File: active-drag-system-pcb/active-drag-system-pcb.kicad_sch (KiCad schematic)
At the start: 39 parts, among them J1 USB_B_Micro, J2 Conn_01x02, J3 Conn_02x18_Odd_Even, J4 Conn_02x18_Odd_Even, U1 NCP1117-3.3_SOT223, U2 W25Q128JVS, U3 RP2040, U4 CYW43439KUBGT, U5 ADXL375BCCZ, U6 IIM-42653, U7 LSM6DSV16XTR, U8 NCP1117ST50T3G, Y1 ABM8-272-T3

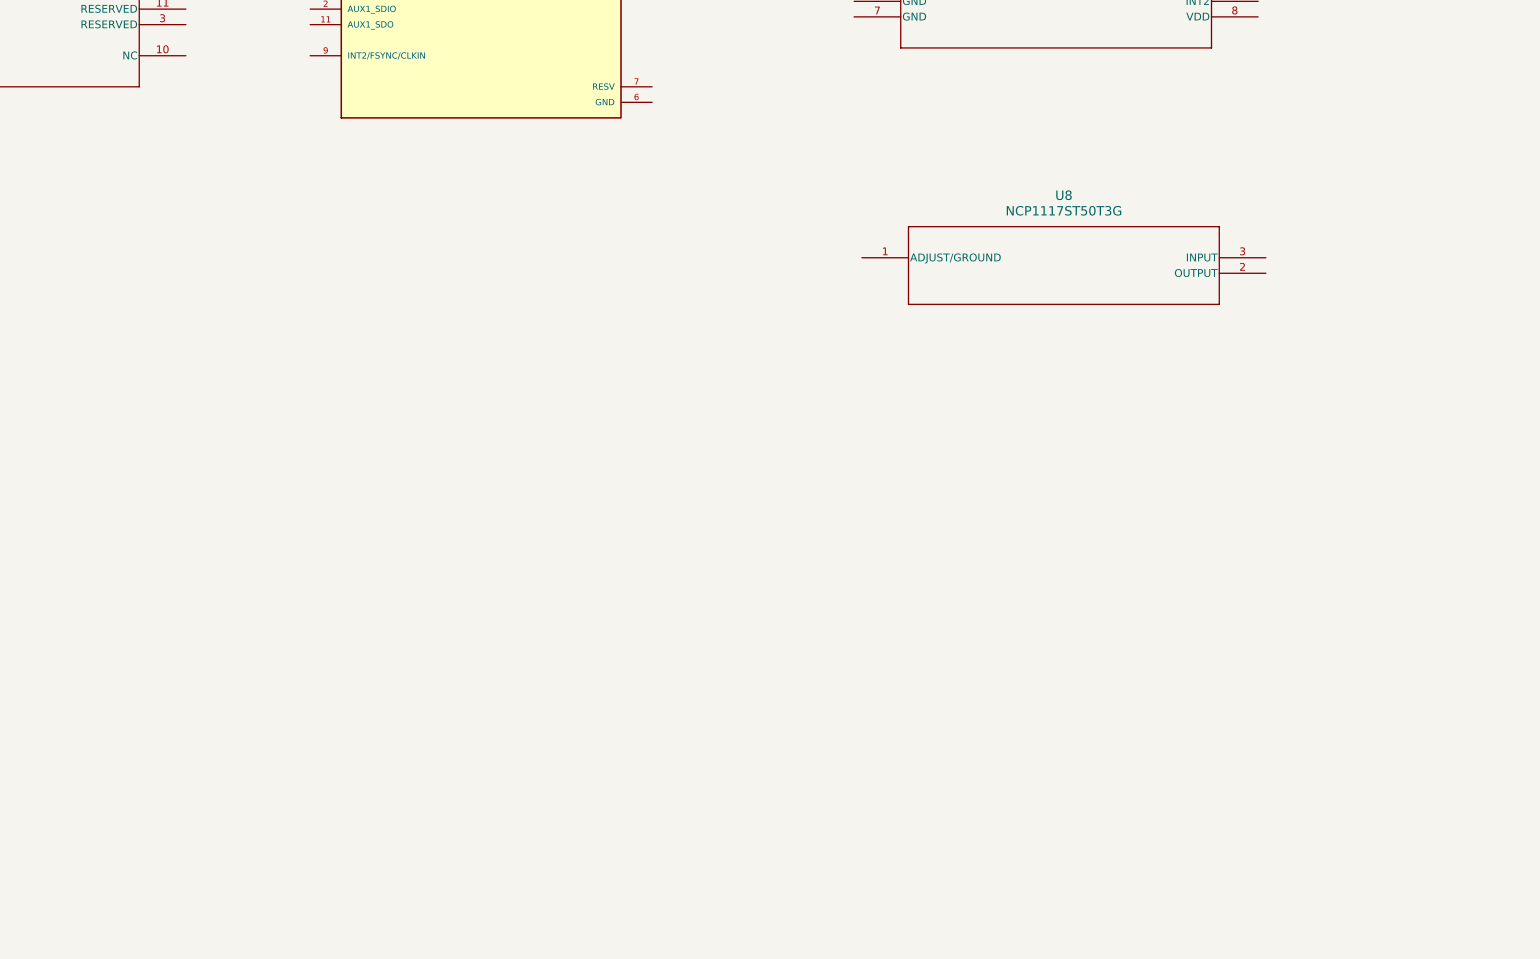
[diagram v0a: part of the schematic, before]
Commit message: 3.3v ldo and 5v+8.4v switching schematic
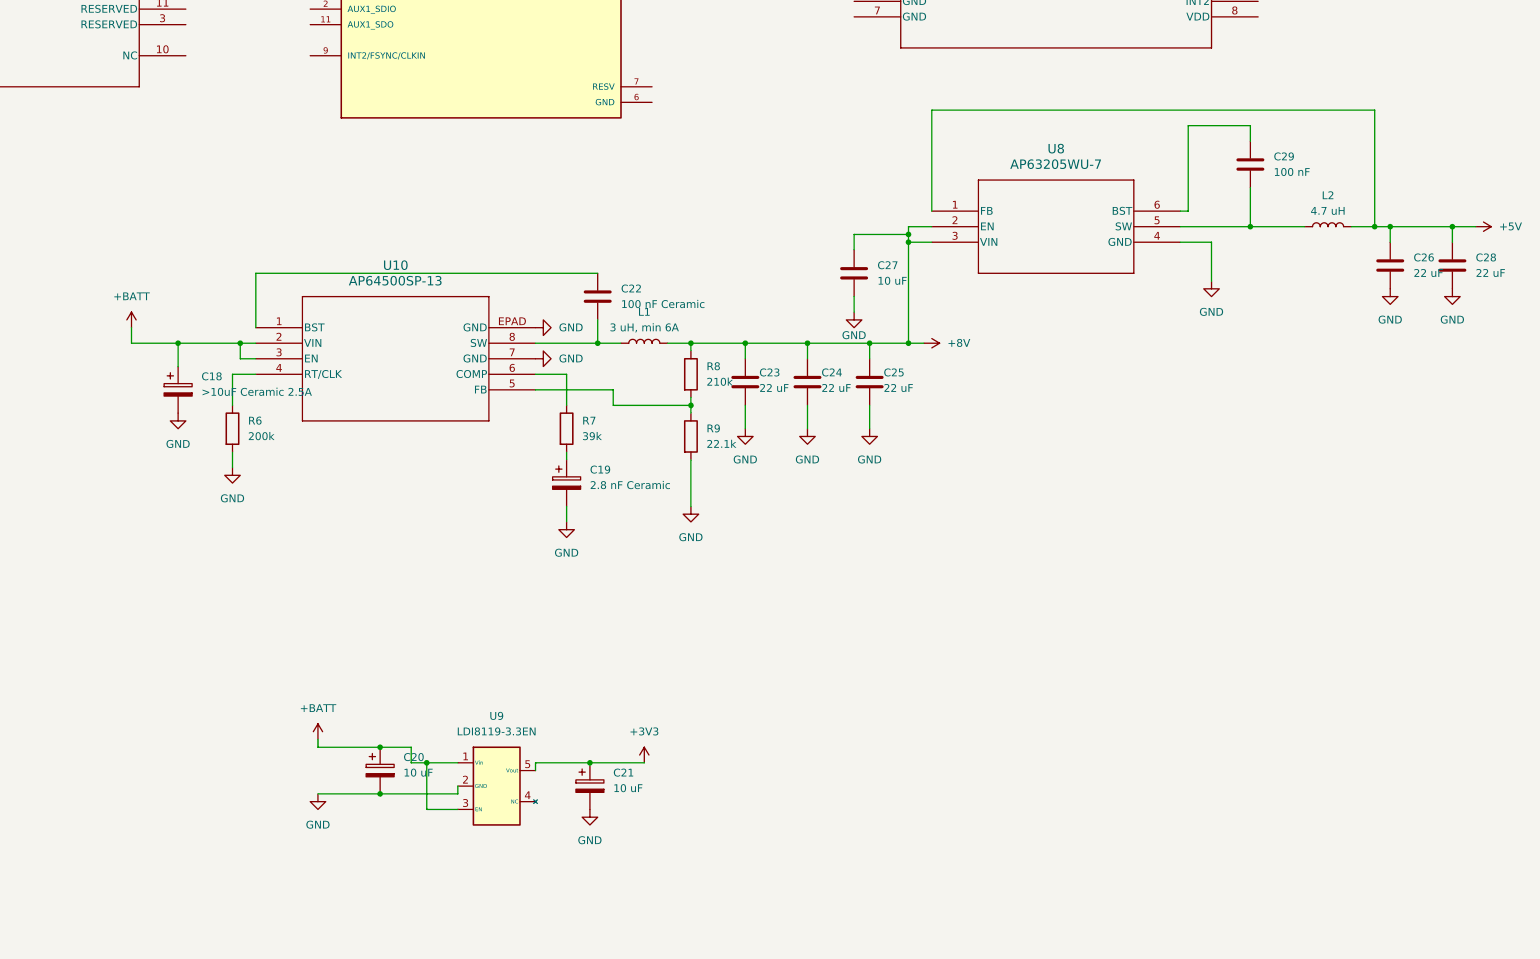
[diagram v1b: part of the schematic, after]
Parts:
- removed U8: NCP1117ST50T3G, SOT223-3_ONS, symbol ADS_Library:NCP1117ST50T3G
- added C18: >10uF Ceramic 2.5A, symbol Device:C_Polarized
- added C19: 2.8 nF Ceramic, symbol Device:C_Polarized
- added C20, C21: 10 uF, symbol Device:C_Polarized
- added C22: 100 nF Ceramic, symbol Device:C
- added C23, C24, C25, C26, C28: 22 uF, symbol Device:C
- added C27: 10 uF, symbol Device:C
- added C29: 100 nF, symbol Device:C
- added L1: 3 uH, min 6A, symbol Device:L
- added L2: 4.7 uH, symbol Device:L
- added R6: 200k, symbol Device:R
- added R7: 39k, symbol Device:R
- added R8: 210k, symbol Device:R
- added R9: 22.1k, symbol Device:R
- added U10: AP64500SP-13, SO-8EP_DIO, symbol ADS_Library:AP64500SP-13
- added U8: AP63205WU-7, SOIC_05WU-7_DIO, symbol ADS_Library:AP63205WU-7
- added U9: LDI8119-3.3EN, symbol ADS_Library:LDI8119-3.3EN
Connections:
- net +3V3: now also C21.1, U9.5 (Vout)
- net GND: now also C18.2, C19.2, C20.2, C21.2, C23.2, C24.2, C25.2, C26.2, C27.2, C28.2, R6.2, R9.2, U10.7 (GND), U10.EPAD (GND), U8.4 (GND), U9.2 (GND)
- new net: R8.2, R9.1, U10.5 (FB)
- new net: C22.1, U10.1 (BST)
- new net: C22.2, L1.1, U10.8 (SW)
- new net: R7.1, U10.6 (COMP)
- new net: C19.1, R7.2
- new net: C29.2, L2.1, U8.5 (SW)
- new net: C29.1, U8.6 (BST)
- new net: R6.1, U10.4 (RT/CLK)
- new net +5V: C26.1, C28.1, L2.2, U8.1 (FB)
- new net +8V: C23.1, C24.1, C25.1, C27.1, L1.2, R8.1, U8.2 (EN), U8.3 (VIN)
- new net +BATT: C18.1, C20.1, U10.2 (VIN), U10.3 (EN), U9.1 (Vin), U9.3 (EN)

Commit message: fixed power nets
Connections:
- net +5V: now also C20.1, U9.1 (Vin), U9.3 (EN)
- net +8V: no longer C27.1, U8.2 (EN), U8.3 (VIN)
- net +BATT: now also C27.1, U8.2 (EN), U8.3 (VIN); no longer C20.1, U9.1 (Vin), U9.3 (EN)
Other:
- moved on the sheet: C26, C27, C28, C29, L2, U8

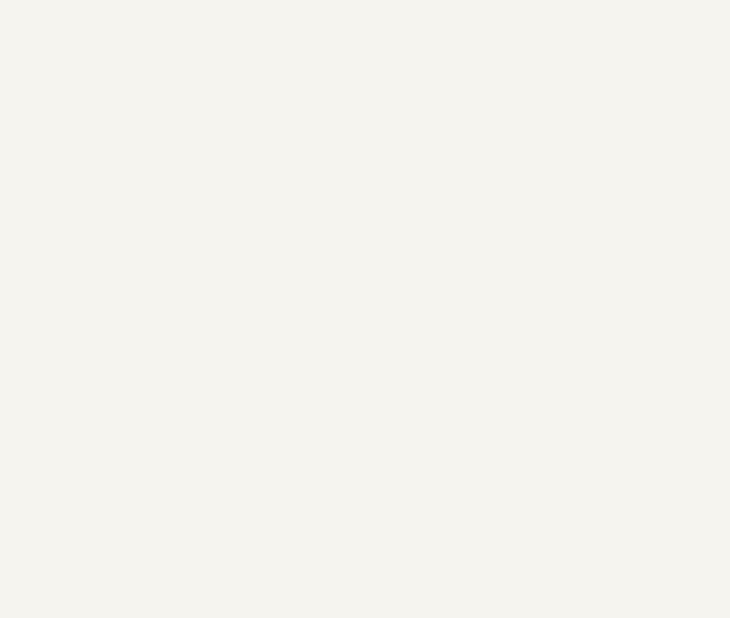
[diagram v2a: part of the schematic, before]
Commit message: First Phase Motor Control
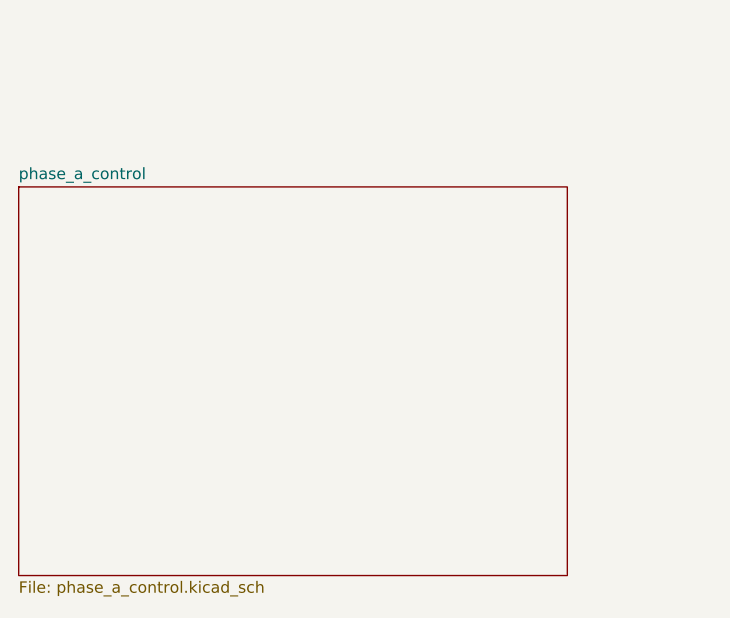
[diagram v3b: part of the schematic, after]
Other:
- added sheet phase_a_control (phase_a_control.kicad_sch)
- company: (none) -> Rocketry at Virginia Tech
- title: (none) -> Active Drag System

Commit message: Add other two phases; remove CYW43 for scope reasons
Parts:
- removed U4: CYW43439KUBGT, SG-XFWLB-63-800, symbol ADS_Library:CYW43439KUBGT
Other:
- added sheet phase_b_control (phase_b_control.kicad_sch)
- added sheet phase_c_control (phase_c_control.kicad_sch)
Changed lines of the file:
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@@
-	)
-	(symbol
-		(lib_id "ADS_Library:CYW43439KUBGT")
-		(at 379.73 66.04 0)
-		(unit 1)
-		(exclude_from_sim no)
-		(in_bom yes)
-		(on_board yes)
-		(dnp no)
-		(fields_autoplaced yes)
-		(property "Reference" "U4"
-			(at 435.61 55.88 0)
-			(effects
-				(font
-					(size 1.524 1.524)
-				)
-			)
-		)
-		(property "Value" "CYW43439KUBGT"
-			(at 435.61 58.42 0)
-			(effects
-				(font
-					(size 1.524 1.524)
-				)
-			)
-		)
-		(property "Footprint" "SG-XFWLB-63-800"
-			(at 379.73 66.04 0)
-			(effects
-				(font
-					(size 1.27 1.27)
-					(italic yes)
-				)
-				(hide yes)
-			)
-		)
-		(property "Datasheet" "CYW43439KUBGT"
-			(at 379.73 66.04 0)
-			(effects
-				(font
-					(size 1.27 1.27)
-					(italic yes)
-				)
-				(hide yes)
-			)
-		)
-		(property "Description" ""
-			(at 379.73 66.04 0)
-			(effects
-				(font
-					(size 1.27 1.27)
-				)
-				(hide yes)
-			)
-		)
-		(pin "G4"
-		)
-		(pin "A1"
-		)
-		(pin "A5"
-		)
-		(pin "J3"
-		)
-		(pin "H1"
-		)
-		(pin "F5"
-		)
-		(pin "C1"
-		)
-		(pin "H2"
-		)
-		(pin "A7"
-		)
-		(pin "C2"
-		)
-		(pin "C6"
-		)
-		(pin "D2"
-		)
-		(pin "C3"
-		)
-		(pin "E1"
-		)
-		(pin "F1"
-		)
-		(pin "D3"
-		)
-		(pin "G1"
-		)
-		(pin "G6"
-		)
-		(pin "C4"
-		)
-		(pin "A6"
-		)
-		(pin "B6"
-		)
-		(pin "B7"
-		)
-		(pin "D6"
-		)
-		(pin "C7"
-		)
-		(pin "E2"
-		)
-		(pin "E3"
-		)
-		(pin "E7"
-		)
-		(pin "F2"
-		)
-		(pin "F6"
-		)
-		(pin "H3"
-		)
-		(pin "H4"
-		)
-		(pin "B5"
-		)
-		(pin "A2"
-		)
-		(pin "G2"
-		)
-		(pin "D4"
-		)
-		(pin "B2"
-		)
-		(pin "E6"
-		)
-		(pin "B1"
-		)
-		(pin "B4"
-		)
-		(pin "F7"
-		)
-		(pin "M4"
-		)
-		(pin "L5"
-		)
-		(pin "M1"
-		)
-		(pin "K2"
-		)
-		(pin "K6"
-		)
-		(pin "J1"
-		)
-		(pin "J6"
-		)
-		(pin "L3"
-		)
-		(pin "J7"
-		)
-		(pin "J2"
-		)
-		(pin "M3"
-		)
-		(pin "K1"
-		)
-		(pin "L4"
-		)
-		(pin "H6"
-		)
-		(pin "M5"
-		)
-		(pin "H7"
-		)
-		(pin "J5"
-		)
-		(pin "L7"
-		)
-		(pin "L2"
-		)
-		(pin "M2"
-		)
-		(pin "M7"
-		)
-		(pin "L6"
-		)
-		(pin "M6"
-		)
-		(instances
-			(project ""
-				(path "/bbbb29dc-aa75-4226-931e-5c4f0b0fc0d6"
-					(reference "U4")
-					(unit 1)
-				)
-			)
-		)
 	)
 	(symbol
@@
 				)
 			)
+		)
+	)
+	(sheet
+		(at 172.72 444.5)
+		(size 60.96 43.18)
+		(fields_autoplaced yes)
+		(stroke
+			(width 0.1524)
+			(type solid)
+		)
+		(fill
+			(color 0 0 0 0.0000)
+		)
+		(property "Sheetname" "phase_b_control"
+			(at 172.72 443.7884 0)
+			(effects
+				(font
+					(size 1.27 1.27)
+				)
+				(justify left bottom)
+			)
+		)
+		(property "Sheetfile" "phase_b_control.kicad_sch"
+			(at 172.72 488.2646 0)
+			(effects
+				(font
+					(size 1.27 1.27)
+				)
+				(justify left top)
+			)
+		)
+		(instances
+			(project "active-drag-system-pcb"
+				(path "/bbbb29dc-aa75-4226-931e-5c4f0b0fc0d6"
+					(page "3")
+				)
+			)
+		)
+	)
+	(sheet
+		(at 247.65 444.5)
+		(size 60.96 43.18)
+		(fields_autoplaced yes)
+		(stroke
+			(width 0.1524)
+			(type solid)
+		)
+		(fill
+			(color 0 0 0 0.0000)
+		)
+		(property "Sheetname" "phase_c_control"
+			(at 247.65 443.7884 0)
+			(effects
+				(font
+					(size 1.27 1.27)
+				)
+				(justify left bottom)
+			)
+		)
+		(property "Sheetfile" "phase_c_control.kicad_sch"
+			(at 247.65 488.2646 0)
+			(effects
+				(font
+					(size 1.27 1.27)
+				)
+				(justify left top)
+			)
+		)
+		(property "Field2" ""
+			(at 247.65 444.5 0)
+			(effects
+				(font
+					(size 1.27 1.27)
+				)
+				(hide yes)
+			)
+		)
+		(instances
+			(project "active-drag-system-pcb"
+				(path "/bbbb29dc-aa75-4226-931e-5c4f0b0fc0d6"
+					(page "4")
+				)
+			)

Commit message: Swapped out regulators for higher current output; removed 8.4 V regulator; now two grounds (power and analog)
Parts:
- removed C17: 10u, Capacitor_SMD:C_0805_2012Metric, symbol Device:C
- removed C18: >10uF Ceramic 2.5A, symbol Device:C_Polarized
- removed C19: 2.8 nF Ceramic, symbol Device:C_Polarized
- removed C20, C21: 10 uF, symbol Device:C_Polarized
- removed C22: 100 nF Ceramic, symbol Device:C
- removed C23, C24, C25, C26, C28: 22 uF, symbol Device:C
- removed C27: 10 uF, symbol Device:C
- removed C29: 100 nF, symbol Device:C
- removed J3, J4: Conn_02x18_Odd_Even, Connector_PinHeader_2.54mm:PinHeader_2x18_P2.54mm_Vertical, symbol Connector_Generic:Conn_02x18_Odd_Even
- removed L2: 4.7 uH, symbol Device:L
- removed R9: 22.1k, symbol Device:R
- removed U1: NCP1117-3.3_SOT223, Package_TO_SOT_SMD:SOT-223-3_TabPin2, symbol Regulator_Linear:NCP1117-3.3_SOT223
- removed U10: AP64500SP-13, SO-8EP_DIO, symbol ADS_Library:AP64500SP-13
- removed U8: AP63205WU-7, SOIC_05WU-7_DIO, symbol ADS_Library:AP63205WU-7
- removed U9: LDI8119-3.3EN, symbol ADS_Library:LDI8119-3.3EN
- added C10, C7, C8, C9: 22uF, symbol Device:C
- added C11, C12, C2, C3: 10uF, symbol Device:C
- added C5: 0.1uF, symbol Device:C
- added C6: 22pF, symbol Device:C
- added J1: Conn_01x02_Socket, symbol Connector:Conn_01x02_Socket
- added R1: 560k, symbol Device:R
- added R2: 80k, symbol Device:R
- added R3: 100k, symbol Device:R
- added R4: 0, symbol Device:R
- added R5: 150k, symbol Device:R
- added U1: TPS51386RJNR, TPS51386RJNR:VREG_TPS51386RJNR, symbol TPS51386RJNR:TPS51386RJNR
- added U2: LD39200PU33R, SON_DFN6_3X3_STM, symbol 2024-10-13_18-34-19:LD39200PU33R
- added U3, U4: PMEG3050EP_115, PMEG3050EP_115:SODFL4725X110N, symbol PMEG3050EP_115:PMEG3050EP_115
- C1: value 10u -> 0.1uF; footprint Capacitor_SMD:C_0805_2012Metric -> (none)
- C4: value 10u -> 1uF; footprint Capacitor_SMD:C_0805_2012Metric -> (none)
- L1: value 3 uH, min 6A -> 1.5uH
- R6: value 200k -> 0
- R7: value 39k -> 20k
- R8: value 210k -> 100k
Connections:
- net +3V3: now also C12.1, U2.1 (OUT), U2.2 (ADJ/SENSE); no longer C4.1
- net +5V: now also L1.2, C10.1, C6.2, C7.1, C8.1, C9.1, R5.2, U4.2 (A)
- net +BATT: now also C1.1, C2.1, C3.1, J1.1 (Pin_1), R1.1, U1.1 (VIN)
- net GND: no longer C1.2, C10.2, C11.2, C12.2, C13.2, C14.2, C15.2, C16.2, C4.2, C5.2, C6.2, C7.2, C8.2, C9.2, R6.2, U3.19 (TESTEN), U3.57 (GND)
- net VBUS: now also U3.2 (A); no longer C1.1
- net at R8.2: now also U2.5 (EN)
- net at L1.1: now also C5.2, U1.7 (SW)
- net at R7.1: now also R6.1, R5.1, U1.4 (FB)
- net -BATT: now reaches R7.2
- net -BATT: now also C1.2, C10.2, C11.2, C12.2, C13.2, C14.2, C15.2, C16.2, C4.2, C5.2, C6.2, C7.2, C8.2, C9.2, U3.19 (TESTEN), U3.57 (GND), C10.2, C11.2, C12.2, C2.2, C3.2, C7.2, C8.2, C9.2, J1.2 (Pin_2), R2.1, U1.10 (AGND), U1.2 (PGND), U2.3 (GND), U2.7 (GND)
- net +8V: no longer names the net of R8.1
- net +8V: now also C11.1, U2.6 (IN), U3.1 (K), U4.1 (K); no longer L1.2
- new net: R4.1, U1.8 (VBST)
- new net: C5.1, R4.2
- new net: R1.2, R2.2, U1.11 (EN)
- new net: R3.2, U1.3 (PG)
- new net: C4.1, R3.1, U1.9 (VCC)
- new net: C6.1, R6.2
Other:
- note added: "12 MHz"
- note removed: "IOs"
- moved on the sheet: J1

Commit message: Copy pasting Pico Schematic
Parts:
- removed C10, C8: 1u, Capacitor_SMD:C_0402_1005Metric, symbol Device:C
- removed C11, C12, C5, C6, C7, C9: 100n, Capacitor_SMD:C_0402_1005Metric, symbol Device:C
- removed C2, C3: 15p, Capacitor_SMD:C_0402_1005Metric, symbol Device:C
- removed J2: Conn_01x02, Connector_PinHeader_2.54mm:PinHeader_1x02_P2.54mm_Vertical, symbol Connector_Generic:Conn_01x02
- removed R1, R5: 1k, Resistor_SMD:R_0402_1005Metric, symbol Device:R
- removed R2: DNF, Resistor_SMD:R_0402_1005Metric, symbol Device:R
- removed R3, R4: 27, Resistor_SMD:R_0402_1005Metric, symbol Device:R
- removed U2: W25Q128JVS, Package_SO:SOIC-8_5.23x5.23mm_P1.27mm, symbol Memory_Flash:W25Q128JVS
- removed U3: RP2040, RP2040_minimal:RP2040-QFN-56, symbol MCU_RaspberryPi_RP2040:RP2040
- removed U5: ADXL375BCCZ, LGA_CC-14-1_ADI, symbol ADS_Library:ADXL375BCCZ
- removed U6: IIM-42653, IIM-42653:PQFN50P250X300X97-14N, symbol ADS_Library:IIM-42653
- removed U7: LSM6DSV16XTR, LGA14L_LSM6_STM, symbol ADS_Library:LSM6DSV16XTR
- added C17, C18: 2.2uF, symbol Device:C
- added C19, C20, C21, C22, C23, C24, C27: 100n, symbol Device:C
- added C25, C26: 15p, symbol Device:C
- added D7: WL-SMCW_0603, WL-SMCW_0603:WL-SMCW_0603, symbol WL-SMCW_0603:WL-SMCW_0603
- added R28, R29: 27, symbol Device:R
- added R30: 1, symbol Device:R
- added R31: 200, symbol Device:R
- added R32, R33: 1k, symbol Device:R
- added R9: 100, symbol Device:R
- added SW1: PTS815 SJM 250 SMTR LFS, SW4_PTS815 SJM 250 SMTR LFS_CNK, symbol PTS815_SJM_250_SMTR_LFS:PTS815_SJM_250_SMTR_LFS
- added U5: RP2040, Package_DFN_QFN:QFN-56-1EP_7x7mm_P0.4mm_EP3.2x3.2mm, symbol MCU_RaspberryPi:RP2040
- added U6: W25Q128JVS, Package_SO:SOIC-8_5.23x5.23mm_P1.27mm, symbol Memory_Flash:W25Q128JVS
- C13: value 100n -> 2.2uF
- C14, C15: footprint Capacitor_SMD:C_0402_1005Metric -> (none)
- C16: value 100n -> 2.2uF; footprint Capacitor_SMD:C_0402_1005Metric -> (none)
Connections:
- net +1V1: now also C14.1, C16.1, C22.1, U5.23 (DVDD), U5.45 (VREG_VOUT), U5.50 (DVDD)
- net +3V3: now also C17.1, C19.1, C20.1, C21.1, C23.1, C24.1, C27.1, R31.1, U5.1 (IOVDD), U5.10 (IOVDD), U5.22 (IOVDD), U5.33 (IOVDD), U5.42 (IOVDD), U5.44 (VREG_IN), U5.48 (USB_VDD), U5.49 (IOVDD), U6.8 (VCC); no longer C14.1, C16.1
- net -BATT: now also Y1.2, Y1.4, C17.2, C18.2, C19.2, C20.2, C21.2, C22.2, C23.2, C24.2, C25.2, C26.2, C27.2, D7.1, SW1.3, SW1.4, U5.19 (TESTEN), U5.57 (GND), U6.4 (GND)
- net GND: no longer Y1.2, Y1.4
- net GPIO0: now also U5.2 (GPIO0)
- net GPIO1: now also U5.3 (GPIO1)
- net GPIO10: now also U5.13 (GPIO10)
- net GPIO11: now also U5.14 (GPIO11)
- net GPIO12: now also U5.15 (GPIO12)
- net GPIO13: now also U5.16 (GPIO13)
- net GPIO14: now also U5.17 (GPIO14)
- net GPIO15: now also U5.18 (GPIO15)
- net GPIO16: now also U5.27 (GPIO16)
- net GPIO17: now also U5.28 (GPIO17)
- net GPIO18: now also U5.29 (GPIO18)
- net GPIO19: now also U5.30 (GPIO19)
- net GPIO2: now also U5.4 (GPIO2)
- net GPIO20: now also U5.31 (GPIO20)
- net GPIO21: now also U5.32 (GPIO21)
- net GPIO22: now also U5.34 (GPIO22)
- net GPIO23: now also U5.35 (GPIO23)
- net GPIO24: now also U5.36 (GPIO24)
- net GPIO25: now also R9.2, U5.37 (GPIO25)
- net GPIO26_ADC0: now also U5.38 (GPIO26_ADC0)
- net GPIO27_ADC1: now also U5.39 (GPIO27_ADC1)
- net GPIO28_ADC2: now also U5.40 (GPIO28_ADC2)
- net GPIO29_ADC3: now also U5.41 (GPIO29_ADC3)
- net GPIO3: now also U5.5 (GPIO3)
- net GPIO4: now also U5.6 (GPIO4)
- net GPIO5: now also U5.7 (GPIO5)
- net GPIO6: now also U5.8 (GPIO6)
- net GPIO7: now also U5.9 (GPIO7)
- net GPIO8: now also U5.11 (GPIO8)
- net GPIO9: now also U5.12 (GPIO9)
- net QSPI_SCLK: now also U5.52 (QSPI_SCLK), U6.6 (CLK)
- net QSPI_SD0: now also U5.53 (QSPI_SD0), U6.5 (DI(IO0))
- net QSPI_SD1: now also U5.55 (QSPI_SD1), U6.2 (DO(IO1))
- net QSPI_SD2: now also U5.54 (QSPI_SD2), U6.3 (IO2)
- net QSPI_SD3: now also U5.51 (QSPI_SD3), U6.7 (IO3)
- net QSPI_SS: now also R33.2, U5.56 (QSPI_SS), U6.1 (~{CS})
- net RUN: now also U5.26 (RUN)
- net SWCLK: now also U5.24 (SWCLK)
- net SWD: now also U5.25 (SWD)
- net USB_D+: now also R28.1
- net USB_D-: now also R29.1
- net XIN: now also C26.1, U5.20 (XIN)
- net XOUT: now also R32.1, U5.21 (XOUT)
- net at Y1.3: now also C25.1, R32.2
- new net: C18.1, R30.2, U5.43 (ADC_AVDD)
- new net: R33.1, SW1.1, SW1.2
- new net: D7.2, R9.1
- new net: R29.2, U5.46 (USB_DM)
- new net: R28.2, U5.47 (USB_DP)
- new net ADC_VREF: R30.1, R31.2
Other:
- note removed: "Make sure C10 is close to pin 44 of RP2040"
- note removed: "Make sure C8 is close to pin 45 of RP2040"
- note removed: "Make sure R3 and R4 are close to RP2040"
- moved on the sheet: Y1
